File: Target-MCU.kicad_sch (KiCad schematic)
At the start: 18 parts, among them Q6 DMG1012UW-7, SW5 12V 50mA, U4 CH32V003F4P6

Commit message: Adapt project to KiCAD 8
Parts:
- U4: footprint Package_SO:TSSOP-20_4.4x6.5mm_P0.65mm -> Tiny_Scarab:TSSOP-20_4.4x6.5mm_P0.65mm

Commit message: Apply JLCPCB rotations and offsets to components
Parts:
- Q6: JLCPCB Rotation Offset (none) -> 180
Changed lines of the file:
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@@
 	(title_block
 		(title "Tiny Scarab")
-		(date "2024-01-30")
+		(date "2024-03-04")
 		(rev "0.2")
 		(company "Embeetle")
@@
 			)
 		)
-		(property "Description" ""
+		(property "Description" "32-bit general-purpose RISC-V MCU"
 			(at 118.11 57.15 0)
 			(effects
@@
 			)
 		)
-		(property "Description" ""
+		(property "Description" "Unpolarized capacitor"
 			(at 100.33 40.64 0)
 			(effects
@@
 			)
 		)
-		(property "Description" ""
+		(property "Description" "Power symbol creates a global label with name \"GND\" , ground"
 			(at 82.55 49.53 0)
 			(effects
@@
 			)
 		)
-		(property "Description" ""
+		(property "Description" "Power symbol creates a global label with name \"GND\" , ground"
 			(at 191.77 64.77 0)
 			(effects
@@
 			)
 		)
-		(property "Description" ""
+		(property "Description" "Resistor"
 			(at 191.77 43.18 0)
 			(effects
@@
 			)
 		)
-		(property "Description" ""
+		(property "Description" "Resistor"
 			(at 29.21 109.22 0)
 			(effects
@@
 			)
 		)
-		(property "Description" ""
+		(property "Description" "Power symbol creates a global label with name \"GND\" , ground"
 			(at 121.92 95.25 0)
 			(effects
@@
 			)
 		)
-		(property "Description" ""
+		(property "Description" "Power symbol creates a global label with name \"+5V\""
 			(at 38.1 82.55 0)
 			(effects
@@
 			)
 		)
-		(property "Description" ""
+		(property "Description" "TVS bidirectional, 6V, 3.5pF"
 			(at 180.34 55.88 0)
 			(effects
@@
 			)
 		)
-		(property "Description" ""
+		(property "Description" "Unpolarized capacitor"
 			(at 129.54 100.33 0)
 			(effects
@@
 			)
 		)
-		(property "Description" ""
+		(property "Description" "Unpolarized capacitor"
 			(at 95.25 40.64 0)
 			(effects
@@
 			)
 		)
-		(property "Description" ""
+		(property "Description" "Power symbol creates a global label with name \"VDD\""
 			(at 35.56 44.45 0)
 			(effects
@@
 			)
 		)
-		(property "Description" ""
+		(property "Description" "Power symbol creates a global label with name \"GND\" , ground"
 			(at 35.56 46.99 0)
 			(effects
@@
 			)
 		)
-		(property "Description" ""
+		(property "Description" "Resistor"
 			(at 175.26 48.26 0)
 			(effects
@@
 			)
 		)
-		(property "Description" ""
+		(property "Description" "Crystal 24MHz 20pF ±20ppm"
 			(at 140.97 93.98 0)
 			(effects
@@
 			)
 		)
-		(property "Description" ""
+		(property "Description" "Power symbol creates a global label with name \"GND\" , ground"
 			(at 147.32 95.25 0)
 			(effects
@@
 			)
 		)
-		(property "Description" ""
+		(property "Description" "Power symbol creates a global label with name \"VDD\""
 			(at 82.55 33.02 0)
 			(effects
@@
 			)
 		)
-		(property "Description" ""
+		(property "Description" "Power symbol creates a global label with name \"GND\" , ground"
 			(at 27.94 125.73 0)
 			(effects
@@
 			)
 		)
-		(property "Description" ""
+		(property "Description" "Unpolarized capacitor"
 			(at 90.17 40.64 0)
 			(effects
@@
 			)
 		)
-		(property "Description" ""
+		(property "Description" "Unpolarized capacitor"
 			(at 186.69 55.88 0)
 			(effects
@@
 			)
 		)
-		(property "Description" ""
+		(property "Description" "LED green 0603"
 			(at 38.1 88.9 0)
 			(effects
@@
 			)
 		)
-		(property "Description" ""
+		(property "Description" "NO push button, 12V, 50mA"
 			(at 191.77 54.61 0)
 			(effects
@@
 			)
 		)
-		(property "Description" ""
+		(property "Description" "Unpolarized capacitor"
 			(at 85.09 40.64 0)
 			(effects
@@
 			)
 		)
-		(property "Description" ""
+		(property "Description" "Resistor"
 			(at 24.13 109.22 0)
 			(effects
@@
 			)
 		)
-		(property "Description" ""
+		(property "Description" "Power symbol creates a global label with name \"VDD\""
 			(at 191.77 38.1 0)
 			(effects
@@
 			)
 		)
-		(property "Description" ""
+		(property "Description" "Resistor"
 			(at 38.1 101.6 0)
 			(effects
@@
 			)
 		)
-		(property "Description" ""
+		(property "Description" "Power symbol creates a global label with name \"GND\" , ground"
 			(at 134.62 95.25 0)
 			(effects
@@
 			)
 		)
-		(property "Description" ""
+		(property "Description" "Unpolarized capacitor"
 			(at 129.54 86.36 0)
 			(effects
@@
 			)
 		)
-		(property "Description" ""
+		(property "Description" "NMOS 20V, 1A"
 			(at 35.56 114.3 0)
 			(effects
@@
 			(effects
 				(font
+					(size 1.27 1.27)
+				)
+				(hide yes)
+			)
+		)
+		(property "JLCPCB Rotation Offset" "180"
+			(at 35.56 114.3 0)
+			(effects
+				(font

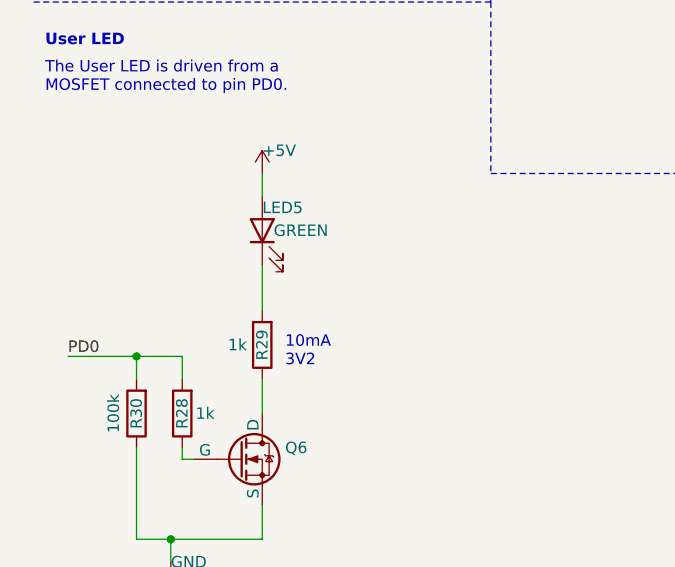
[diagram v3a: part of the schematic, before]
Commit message: Add user LED
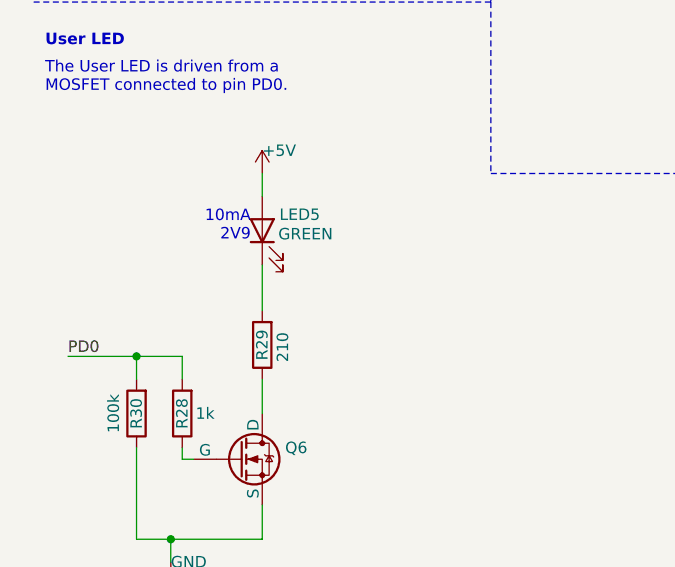
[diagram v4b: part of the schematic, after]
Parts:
- removed LED5: GREEN, Tiny_Scarab:LED_0603_CSL0902ET, symbol Tiny_Scarab:LED_GREEN_CSL0902ET
- added LED5: GREEN, Tiny_Scarab:LED_D3.0mm_green, symbol Tiny_Scarab:LED_GREEN_XSW24061001
- R29: value 1k -> 210; JLCPCB Part # C11702 -> C25090; MPN 0402WGF1001TCE -> 0402WGF2100TCE
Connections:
- net +5V: now also LED5.2 (A)
- net at R29.2: now also LED5.1 (K)
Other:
- note added: "10mA 2V9"
- note removed: "10mA 3V2"
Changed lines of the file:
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@@
 		)
 	)
-	(text "10mA\n3V2"
-		(exclude_from_sim no)
-		(at 40.64 104.14 0)
-		(effects
-			(font
-				(size 1.27 1.27)
-			)
-			(justify left bottom)
-		)
-	)
 	(text "RST_CH32V003"
 		(exclude_from_sim no)
@@
 		)
 	)
+	(text "10mA\n2V9"
+		(exclude_from_sim no)
+		(at 36.83 90.17 0)
+		(effects
+			(font
+				(size 1.27 1.27)
+			)
+			(justify right bottom)
+		)
+	)
 	(text "CH32V003F4P6"
 		(exclude_from_sim no)
@@
 	)
 	(symbol
+		(lib_id "Device:R")
+		(at 38.1 101.6 180)
+		(unit 1)
+		(exclude_from_sim no)
+		(in_bom yes)
+		(on_board yes)
+		(dnp no)
+		(property "Reference" "R29"
+			(at 38.1 101.6 90)
+			(effects
+				(font
+					(size 1.27 1.27)
+				)
+			)
+		)
+		(property "Value" "210"
+			(at 40.386 103.505 90)
+			(effects
+				(font
+					(size 1.27 1.27)
+				)
+				(justify right)
+			)
+		)
+		(property "Footprint" "Resistor_SMD:R_0402_1005Metric_Pad0.72x0.64mm_HandSolder"
+			(at 39.878 101.6 90)
+			(effects
+				(font
+					(size 1.27 1.27)
+				)
+				(hide yes)
+			)
+		)
+		(property "Datasheet" "~"
+			(at 38.1 101.6 0)
+			(effects
+				(font
+					(size 1.27 1.27)
+				)
+				(hide yes)
+			)
+		)
+		(property "Description" "Resistor"
+			(at 38.1 101.6 0)
+			(effects
+				(font
+					(size 1.27 1.27)
+				)
+				(hide yes)
+			)
+		)
+		(property "Manufacturer" "UNI-ROYAL(Uniroyal Elec)"
+			(at 38.1 101.6 0)
+			(effects
+				(font
+					(size 1.27 1.27)
+				)
+				(hide yes)
+			)
+		)
+		(property "MPN" "0402WGF2100TCE"
+			(at 38.1 101.6 90)
+			(effects
+				(font
+					(size 1.27 1.27)
+				)
+				(hide yes)
+			)
+		)
+		(property "JLCPCB Part #" "C25090"
+			(at 38.1 101.6 90)
+			(effects
+				(font
+					(size 1.27 1.27)
+				)
+				(hide yes)
+			)
+		)
+		(pin "2"
+		)
+		(pin "1"
+		)
+		(instances
+			(project "tiny-scarab"
+				(path "/156c5422-ee07-49a4-8263-a2dbd26b90bd/d0c4b0c3-1e7e-4a4c-add3-8d4a3a10843d"
+					(reference "R29")
+					(unit 1)
+				)
+			)
+		)
+	)
+	(symbol
 		(lib_id "Tiny_Scarab:TVS_SP1007-01ETG")
 		(at 180.34 55.88 0)
@@
 	)
 	(symbol
-		(lib_id "Tiny_Scarab:LED_GREEN_CSL0902ET")
+		(lib_id "Tiny_Scarab:LED_GREEN_XSW24061001")
 		(at 38.1 88.9 90)
 		(unit 1)
@@
 		(dnp no)
 		(property "Reference" "LED5"
-			(at 38.1 86.36 90)
+			(at 40.005 87.122 90)
 			(effects
 				(font
@@
 		)
 		(property "Value" "GREEN"
-			(at 39.37 88.9 90)
+			(at 39.878 89.281 90)
 			(effects
 				(font
@@
 			)
 		)
-		(property "Footprint" "Tiny_Scarab:LED_0603_CSL0902ET"
-			(at 17.78 88.9 0)
+		(property "Footprint" "Tiny_Scarab:LED_D3.0mm_green"
+			(at 24.384 88.9 0)
 			(effects
 				(font
@@
 			)
 		)
-		(property "Datasheet" "~"
-			(at 27.94 88.9 0)
+		(property "Datasheet" ""
+			(at 32.766 88.646 0)
 			(effects
 				(font
@@
 			)
 		)
-		(property "Description" "LED green 0603"
-			(at 38.1 88.9 0)
+		(property "Description" "LED GREEN XSW24061001"
+			(at 32.766 88.646 0)
 			(effects
 				(font
@@
 			)
 		)
-		(property "Manufacturer" "ROHM Semicon"
-			(at 20.32 88.9 0)
+		(property "Manufacturer" "Shenzhen Xisheng Microelectronics"
+			(at 26.416 88.9 0)
 			(effects
 				(font
@@
 			)
 		)
-		(property "MPN" "CSL0902ET"
-			(at 22.86 88.9 0)
+		(property "MPN" "xsw24061001"
+			(at 28.702 88.9 0)
 			(effects
 				(font
@@
 			)
 		)
-		(property "JLCPCB Part #" "C7115899"
-			(at 25.4 88.9 0)
+		(property "JLCPCB Part #" "C9900122772"
+			(at 30.734 88.9 0)
 			(effects
 				(font
@@
 			)
 		)
-		(property "Mouser" "755-CSL0902ET1"
-			(at 30.48 88.9 0)
+		(property "DigiKey" ""
+			(at 32.258 88.9 0)
 			(effects
 				(font
@@
 			)
 		)
-		(property "Farnell" "4129807"
-			(at 33.02 88.9 0)
+		(property "Farnell" ""
+			(at 28.194 88.646 0)
 			(effects
 				(font
@@
 			)
 		)
-		(property "DigiKey" "846-CSL0902ET1TR-ND"
-			(at 25.4 88.9 0)
+		(property "Mouser" ""
+			(at 30.226 88.392 0)
 			(effects
 				(font
@@
 			)
 		)
-		(pin "2"
-		)
 		(pin "1"
 		)
+		(pin "2"
+		)
 		(instances
 			(project "tiny-scarab"
@@
 					(unit 1)
 				)
-			)
-		)
-	)
-	(symbol
-		(lib_id "Device:R")
-		(at 38.1 101.6 180)
-		(unit 1)
-		(exclude_from_sim no)
-		(in_bom yes)
-		(on_board yes)
-		(dnp no)
-		(property "Reference" "R29"
-			(at 38.1 101.6 90)
-			(effects
-				(font
-					(size 1.27 1.27)
-				)
-			)
-		)
-		(property "Value" "1k"
-			(at 34.29 101.6 0)
-			(effects
-				(font
-					(size 1.27 1.27)
-				)
-				(justify right)
-			)
-		)
-		(property "Footprint" "Resistor_SMD:R_0402_1005Metric_Pad0.72x0.64mm_HandSolder"
-			(at 39.878 101.6 90)
-			(effects
-				(font
-					(size 1.27 1.27)
-				)
-				(hide yes)
-			)
-		)
-		(property "Datasheet" "~"
-			(at 38.1 101.6 0)
-			(effects
-				(font
-					(size 1.27 1.27)
-				)
-				(hide yes)
-			)
-		)
-		(property "Description" "Resistor"
-			(at 38.1 101.6 0)
-			(effects
-				(font
-					(size 1.27 1.27)
-				)
-				(hide yes)
-			)
-		)
-		(property "Manufacturer" "UNI-ROYAL(Uniroyal Elec)"
-			(at 38.1 101.6 0)
-			(effects
-				(font
-					(size 1.27 1.27)
-				)
-				(hide yes)
-			)
-		)
-		(property "MPN" "0402WGF1001TCE"
-			(at 38.1 101.6 90)
-			(effects
-				(font
-					(size 1.27 1.27)
-				)
-				(hide yes)
-			)
-		)
-		(property "JLCPCB Part #" "C11702"
-			(at 38.1 101.6 90)
-			(effects
-				(font
-					(size 1.27 1.27)
-				)
-				(hide yes)
-			)
-		)
-		(pin "2"
-		)
-		(pin "1"
-		)
-		(instances
-			(project "tiny-scarab"
-				(path "/156c5422-ee07-49a4-8263-a2dbd26b90bd/d0c4b0c3-1e7e-4a4c-add3-8d4a3a10843d"
-					(reference "R29")
-					(unit 1)
-				)

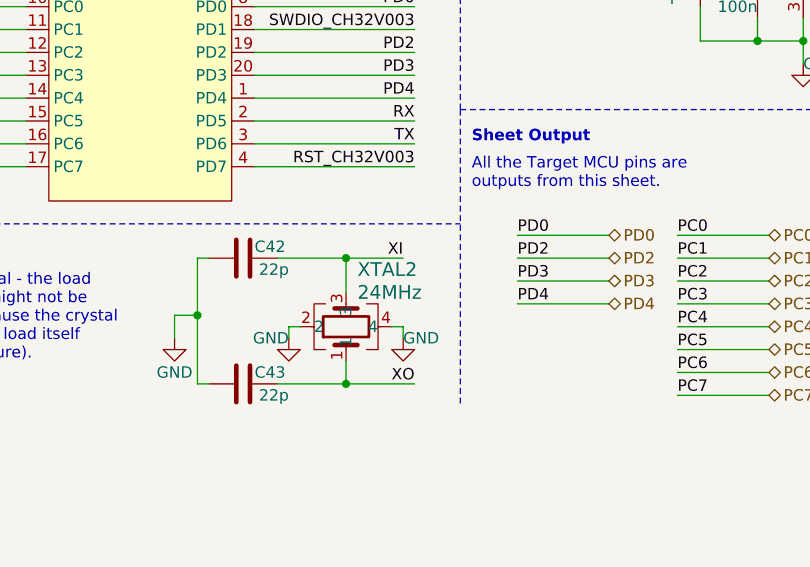
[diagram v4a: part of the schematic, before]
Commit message: Replace 24MHz crystal `M24000J054` with `L327S240V11L`
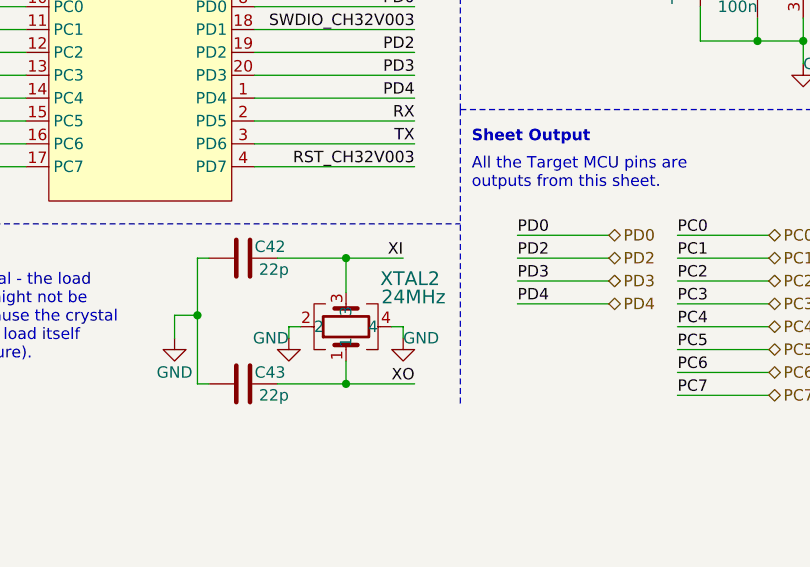
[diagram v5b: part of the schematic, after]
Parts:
- removed XTAL2: 24MHz, Tiny_Scarab:CRYSTAL-SMD3225-4P, symbol Tiny_Scarab:XTAL_M24000J054
- added XTAL2: 24MHz, Tiny_Scarab:CRYSTAL-SMD3225-4P, symbol Tiny_Scarab:XTAL_L327S240V11L
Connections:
- net GND: now also XTAL2.2, XTAL2.4
- net XI: now also XTAL2.3
- net XO: now also XTAL2.1
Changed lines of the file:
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@@
-	)
-	(symbol
-		(lib_id "Tiny_Scarab:XTAL_M24000J054")
-		(at 140.97 93.98 90)
-		(unit 1)
-		(exclude_from_sim no)
-		(in_bom yes)
-		(on_board yes)
-		(dnp no)
-		(property "Reference" "XTAL2"
-			(at 142.24 87.63 90)
-			(effects
-				(font
-					(size 1.524 1.524)
-				)
-				(justify right)
-			)
-		)
-		(property "Value" "24MHz"
-			(at 142.24 90.17 90)
-			(effects
-				(font
-					(size 1.524 1.524)
-				)
-				(justify right)
-			)
-		)
-		(property "Footprint" "Tiny_Scarab:CRYSTAL-SMD3225-4P"
-			(at 109.22 93.98 0)
-			(effects
-				(font
-					(size 1.27 1.27)
-					(italic yes)
-				)
-				(hide yes)
-			)
-		)
-		(property "Datasheet" ""
-			(at 111.76 92.71 0)
-			(effects
-				(font
-					(size 1.27 1.27)
-					(italic yes)
-				)
-				(hide yes)
-			)
-		)
-		(property "Description" "Crystal 24MHz 20pF ±20ppm"
-			(at 140.97 93.98 0)
-			(effects
-				(font
-					(size 1.27 1.27)
-				)
-				(hide yes)
-			)
-		)
-		(property "Manufacturer" "ECEC(ZheJiang E ast Crystal Elec)"
-			(at 111.76 93.98 0)
-			(effects
-				(font
-					(size 1.27 1.27)
-				)
-				(hide yes)
-			)
-		)
-		(property "MPN" "M24000J054"
-			(at 114.3 93.98 0)
-			(effects
-				(font
-					(size 1.27 1.27)
-				)
-				(hide yes)
-			)
-		)
-		(property "JLCPCB Part #" "C279615"
-			(at 116.84 93.98 0)
-			(effects
-				(font
-					(size 1.27 1.27)
-				)
-				(hide yes)
-			)
-		)
-		(property "DigiKey" ""
-			(at 140.97 93.98 0)
-			(effects
-				(font
-					(size 1.27 1.27)
-				)
-				(hide yes)
-			)
-		)
-		(property "Farnell" ""
-			(at 140.97 93.98 0)
-			(effects
-				(font
-					(size 1.27 1.27)
-				)
-				(hide yes)
-			)
-		)
-		(property "Mouser" ""
-			(at 140.97 93.98 0)
-			(effects
-				(font
-					(size 1.27 1.27)
-				)
-				(hide yes)
-			)
-		)
-		(pin "3"
-		)
-		(pin "4"
-		)
-		(pin "1"
-		)
-		(pin "2"
-		)
-		(instances
-			(project "tiny-scarab"
-				(path "/156c5422-ee07-49a4-8263-a2dbd26b90bd/d0c4b0c3-1e7e-4a4c-add3-8d4a3a10843d"
-					(reference "XTAL2")
-					(unit 1)
-				)
-			)
-		)
 	)
 	(symbol
@@
 					(unit 1)
 				)
+			)
+		)
+	)
+	(symbol
+		(lib_id "Tiny_Scarab:XTAL_L327S240V11L")
+		(at 140.97 93.98 90)
+		(unit 1)
+		(exclude_from_sim no)
+		(in_bom yes)
+		(on_board yes)
+		(dnp no)
+		(property "Reference" "XTAL2"
+			(at 148.082 88.646 90)
+			(effects
+				(font
+					(size 1.524 1.524)
+				)
+			)
+		)
+		(property "Value" "24MHz"
+			(at 148.463 90.678 90)
+			(effects
+				(font
+					(size 1.524 1.524)
+				)
+			)
+		)
+		(property "Footprint" "Tiny_Scarab:CRYSTAL-SMD3225-4P"
+			(at 117.094 93.726 0)
+			(effects
+				(font
+					(size 1.27 1.27)
+					(italic yes)
+				)
+				(hide yes)
+			)
+		)
+		(property "Datasheet" ""
+			(at 119.634 92.456 0)
+			(effects
+				(font
+					(size 1.27 1.27)
+					(italic yes)
+				)
+				(hide yes)
+			)
+		)
+		(property "Description" "Crystal 24MHz 22pF ±10ppm"
+			(at 127 93.726 0)
+			(effects
+				(font
+					(size 1.27 1.27)
+				)
+				(hide yes)
+			)
+		)
+		(property "Manufacturer" "Lucki"
+			(at 119.634 93.726 0)
+			(effects
+				(font
+					(size 1.27 1.27)
+				)
+				(hide yes)
+			)
+		)
+		(property "MPN" "L327S240V11L"
+			(at 122.174 93.726 0)
+			(effects
+				(font
+					(size 1.27 1.27)
+				)
+				(hide yes)
+			)
+		)
+		(property "JLCPCB Part #" "C5261157"
+			(at 124.714 93.726 0)
+			(effects
+				(font
+					(size 1.27 1.27)
+				)
+				(hide yes)
+			)
+		)
+		(property "DigiKey" ""
+			(at 140.97 93.98 0)
+			(effects
+				(font
+					(size 1.27 1.27)
+				)
+				(hide yes)
+			)
+		)
+		(property "Farnell" ""
+			(at 140.97 93.98 0)
+			(effects
+				(font
+					(size 1.27 1.27)
+				)
+				(hide yes)
+			)
+		)
+		(property "Mouser" ""
+			(at 140.97 93.98 0)
+			(effects
+				(font
+					(size 1.27 1.27)
+				)
+				(hide yes)
+			)
+		)
+		(pin "3"
+		)
+		(pin "1"
+		)
+		(pin "2"
+		)
+		(pin "4"
+		)
+		(instances
+			(project ""
+				(path "/156c5422-ee07-49a4-8263-a2dbd26b90bd/d0c4b0c3-1e7e-4a4c-add3-8d4a3a10843d"
+					(reference "XTAL2")
+					(unit 1)
+				)
